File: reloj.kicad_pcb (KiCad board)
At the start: 2 copper layers, 81 parts, among them J1 Conn_01x03, J2 USB_B_Mini, SW1 SW_Push, SW2 SW_Push, SW3 SW_Push, U1 LM555, U10 74LS90, U11 74LS90, U12 74LS90, U13 74LS90, U14 74LS08, U15 74LS47, U16 SA04-11SRWA, U17 74LS47, U18 SA04-11SRWA, U19 74LS47, U2 CD4060B, U20 SA04-11SRWA, U21 74LS47, U22 SA04-11SRWA, U3 74LS90, U4 74LS90, U5 74LS90, U6 74LS90, U7 74LS90, U8 74LS92, U9 74LS92, Y1 32768Hz

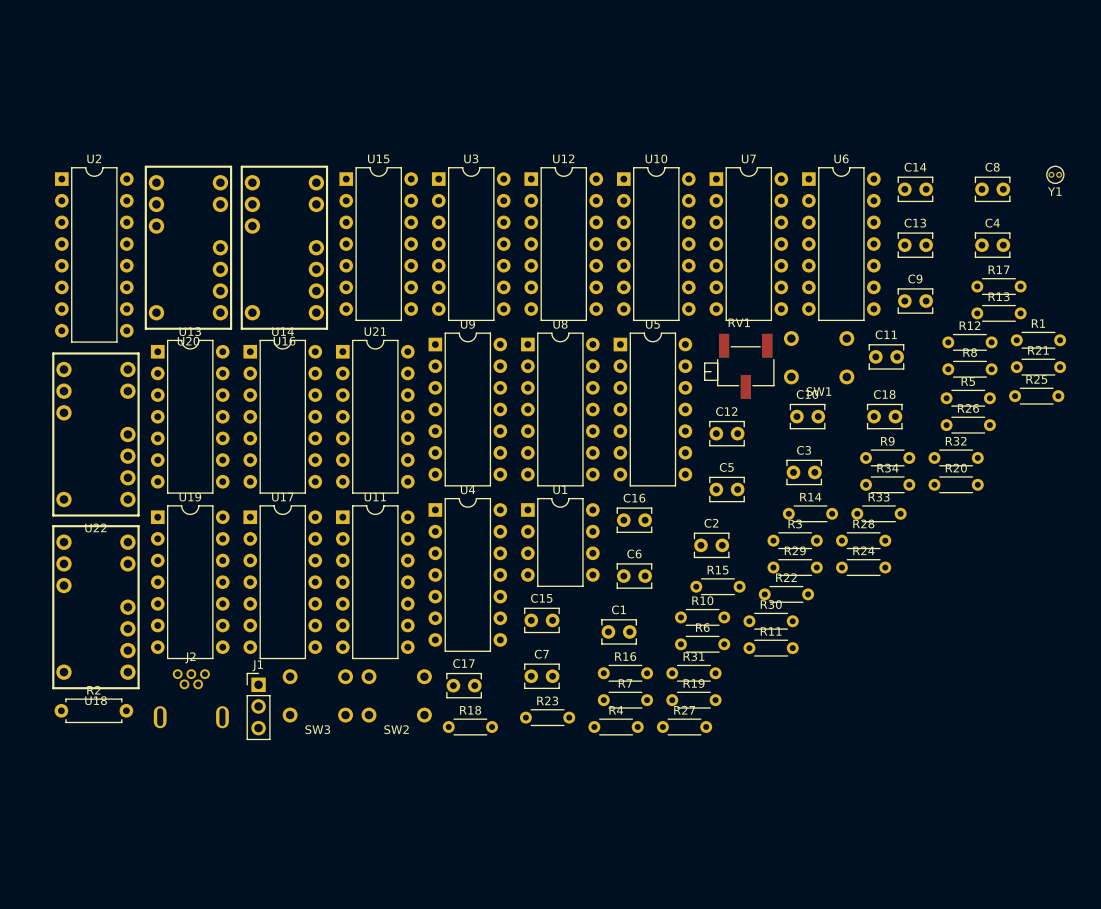
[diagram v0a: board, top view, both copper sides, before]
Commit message: Added most BOM items.
Finished placement on pcb
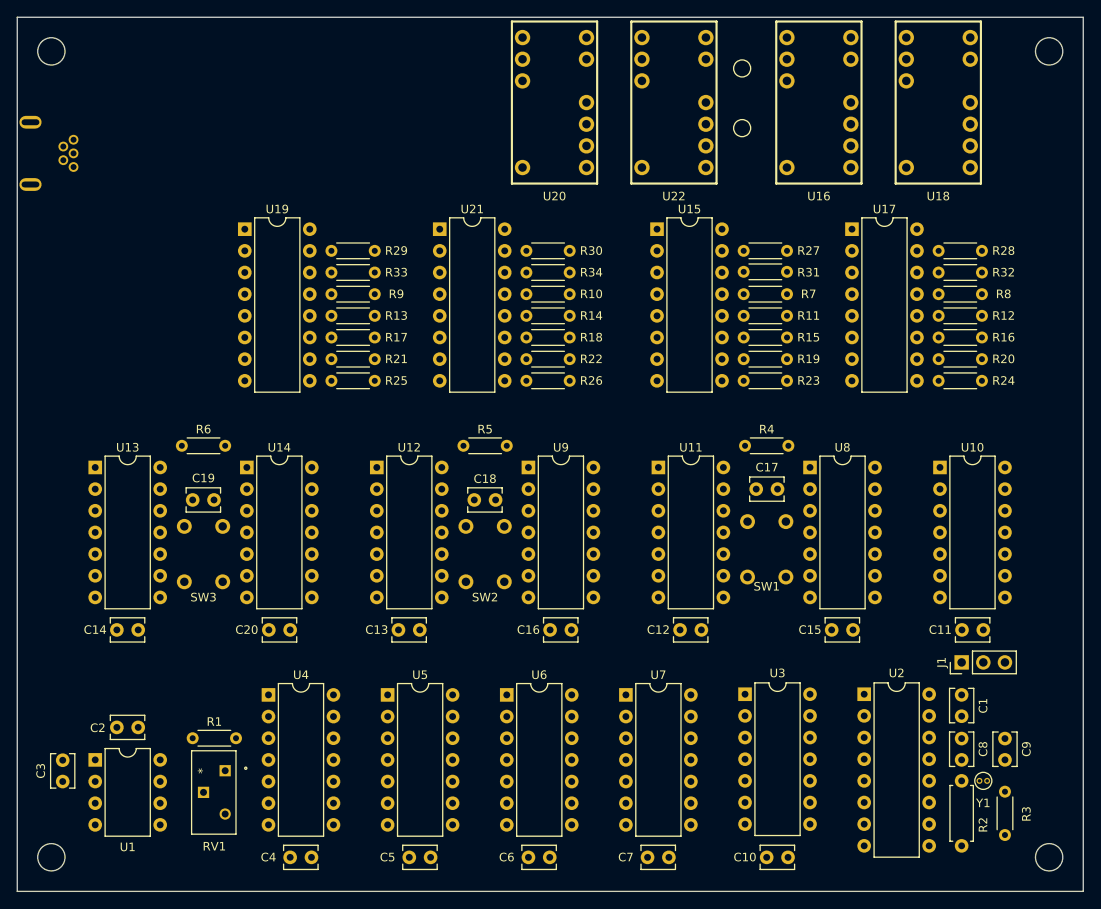
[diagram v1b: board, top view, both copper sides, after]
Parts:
- removed the C12 at (177.0, 93.8)
- removed the C17 at (146.1, 123.4)
- removed the C18 at (195.5, 91.8)
- removed the C8 at (208.1, 65.2)
- added C1: 0.1u, Capacitor_THT:C_Disc_D3.8mm_W2.6mm_P2.50mm, F.Cu at (205.7, 124.5)
- added C10: 0.1u, Capacitor_THT:C_Disc_D3.8mm_W2.6mm_P2.50mm, F.Cu at (182.9, 143.5)
- added C14: 0.1u, Capacitor_THT:C_Disc_D3.8mm_W2.6mm_P2.50mm, F.Cu at (106.7, 116.8)
- added C19: 0.1u, Capacitor_THT:C_Disc_D3.8mm_W2.6mm_P2.50mm, F.Cu at (118.1, 101.6)
- added C20: 0.1u, Capacitor_THT:C_Disc_D3.8mm_W2.6mm_P2.50mm, F.Cu at (124.5, 116.8)
- added C9: 22pf, Capacitor_THT:C_Disc_D3.8mm_W2.6mm_P2.50mm, F.Cu at (210.8, 129.6)
- added REF**: MountingHole_3.2mm_M3, MountingHole:MountingHole_3.2mm_M3, F.Cu at (99.0, 143.5)
- added REF**: MountingHole_3.2mm_M3, MountingHole:MountingHole_3.2mm_M3, F.Cu at (99.0, 49.0)
- added REF**: MountingHole_3.2mm_M3, MountingHole:MountingHole_3.2mm_M3, F.Cu at (216.0, 49.0)
- added REF**: MountingHole_3.2mm_M3, MountingHole:MountingHole_3.2mm_M3, F.Cu at (216.0, 143.5)
- J2: moved to B.Cu
- RV1: footprint Potentiometer_SMD:Potentiometer_Bourns_3269X_Horizontal -> ultra_librarian:3296Y-1-102LF
- U15, U17, U19, U21: footprint Package_DIP:DIP-14_W7.62mm -> Package_DIP:DIP-16_W7.62mm
- moved U18 115.1 mm to (203.0, 55.0)
- moved U2 111.8 mm to (194.3, 124.4)
- moved R1 107.3 mm to (115.6, 129.5)
- moved R2 105.9 mm to (205.7, 134.5), turned to 270 degrees
- moved C5 98.3 mm to (141.0, 143.5)
- moved J1 82.5 mm to (205.7, 120.7), turned to 90 degrees
- moved C3 79.8 mm to (100.3, 134.6), turned to 90 degrees
- moved RV1 79.4 mm to (116.7, 133.4), turned to 90 degrees
- moved U17 78.2 mm to (192.9, 69.8)
- moved U22 78.2 mm to (172.0, 55.0)
- moved R21 75.3 mm to (136.9, 85.1), turned to 180 degrees
- moved R25 75.1 mm to (136.9, 87.6), turned to 180 degrees
- moved C4 74.3 mm to (127.0, 143.5)
- moved Y1 71.6 mm to (208.3, 134.5), turned to 180 degrees
- moved R17 70.9 mm to (136.9, 82.5), turned to 180 degrees
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- renumbered C9 to C11, C10 to C12, C11 to C13, C13 to C15, C14 to C16, C15 to C17, C16 to C18, C1 to C2, C2 to C3, C3 to C4, C4 to C5, C5 to C6, C6 to C7, C7 to C8
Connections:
- R27 pad 2: (no net) -> Net-(R27-Pad2)
- R28 pad 2: (no net) -> Net-(R28-Pad2)
- R29 pad 2: (no net) -> Net-(R29-Pad2)
- R30 pad 2: (no net) -> Net-(R30-Pad2)
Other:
- board outline added: 125 x 102.5 mm
- net class Default: clearance 0.2 -> 0.1524; trace_width 0.25 -> 0.1524; via_dia 0.8 -> 0.508; via_drill 0.4 -> 0.254
- rule trace_clearance: 0.2 -> 0.1524
- rule trace_min: 0.2 -> 0.1524
- rule via_min_drill: 0.3 -> 0.254
- rule via_min_size: 0.4 -> 0.508

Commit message: layout updates
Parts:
- removed the REF** at (99.0, 143.5)
- removed the REF** at (99.0, 49.0)
- removed the REF** at (216.0, 49.0)
- removed the REF** at (216.0, 143.5)
- added REF**: MountingHole_3.2mm_M3, MountingHole:MountingHole_3.2mm_M3, F.Cu at (100.0, 142.5)
- added REF**: MountingHole_3.2mm_M3, MountingHole:MountingHole_3.2mm_M3, F.Cu at (100.0, 50.0)
- added REF**: MountingHole_3.2mm_M3, MountingHole:MountingHole_3.2mm_M3, F.Cu at (215.0, 142.5)
- added REF**: MountingHole_3.2mm_M3, MountingHole:MountingHole_3.2mm_M3, F.Cu at (215.0, 50.0)
- moved J2 23.1 mm to (102.0, 84.0)
- moved C7 2.50 mm to (168.9, 143.5), turned to 0 degrees
- moved R3 1.19 mm to (210.8, 139.7)
- moved U16 1.00 mm to (189.0, 56.0)
- moved U18 1.00 mm to (203.0, 56.0)
- moved U20 1.00 mm to (158.0, 56.0)
- moved U22 1.00 mm to (172.0, 56.0)
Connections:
- U15 pad 6: /DM_Q2 -> /DM_Q3
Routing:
- net GND: track 0.00 -> 667.2 mm
- net CA: track 0.00 -> 653.4 mm, vias 0 -> 1
- net /T_RST: track 0.00 -> 153.5 mm, vias 0 -> 7
- net /H_Q2: track 0.00 -> 75.0 mm, vias 0 -> 1
- net /CLK_DHR: track 0.00 -> 62.9 mm, vias 0 -> 4
- net /DH_Q2: track 0.00 -> 57.9 mm
- net /M_Q1: track 0.00 -> 57.0 mm, vias 0 -> 2
- net /CLK_DMIN: track 0.00 -> 53.7 mm
- net /DH_Q1: track 0.00 -> 53.7 mm
- net /M_Q2: track 0.00 -> 53.4 mm
- net /H_Q1: track 0.00 -> 51.2 mm
- net /CLK_10KHZ: track 0.00 -> 49.8 mm
- net /DM_Q3: track 0.00 -> 48.1 mm
- net Net-(R13-Pad1): track 0.00 -> 47.9 mm, vias 0 -> 2
- net Net-(R17-Pad1): track 0.00 -> 45.6 mm
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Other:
- outline, holes or cut-outs redrawn

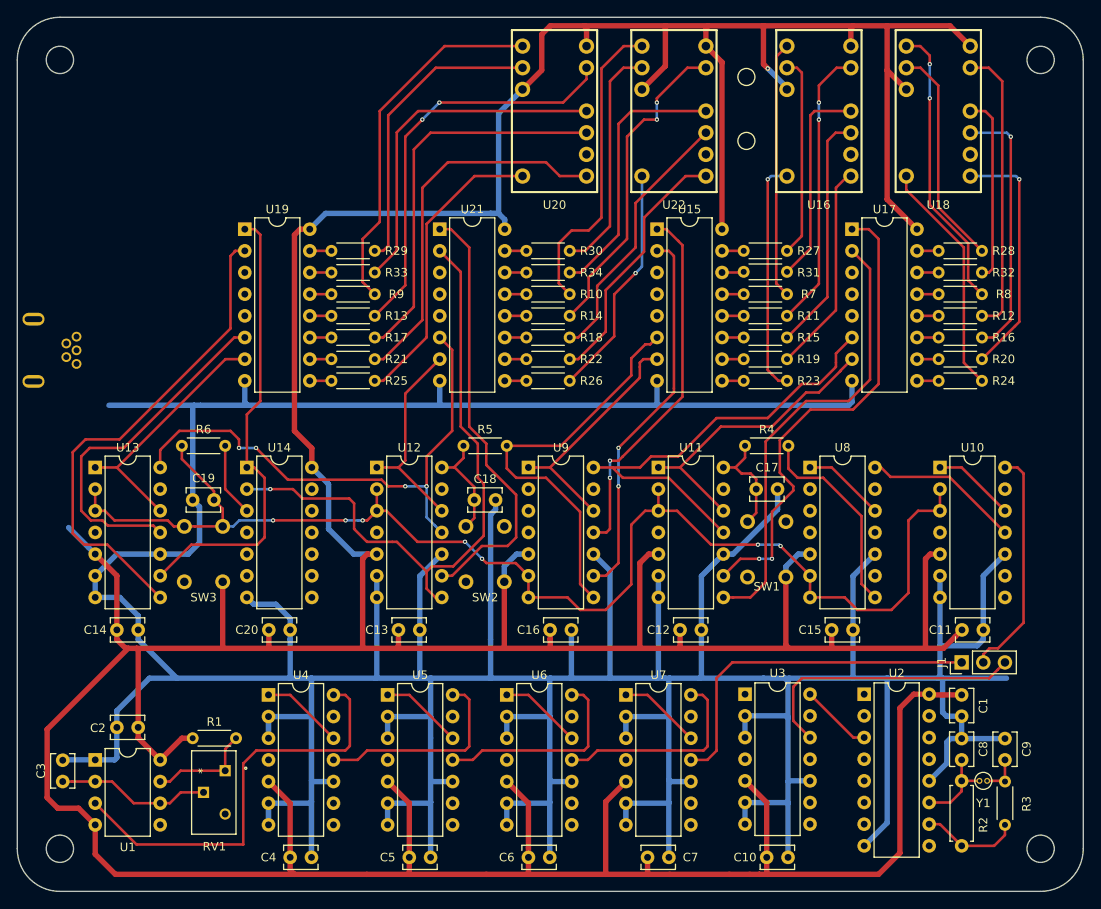
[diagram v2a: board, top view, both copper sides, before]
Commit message: Added 4.7uF cap and cleaned up traces/silkscreen
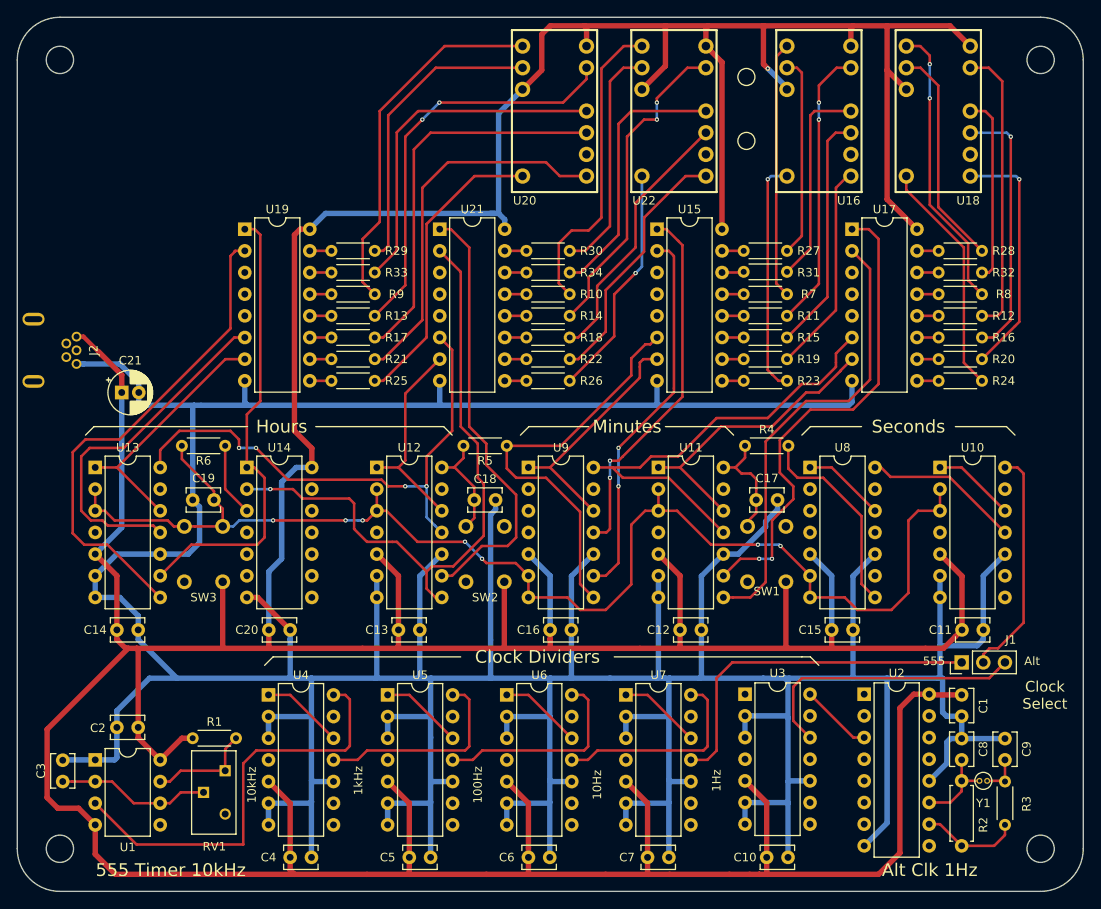
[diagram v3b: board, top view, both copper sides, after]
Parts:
- added C21: 4.7uF, Capacitor_THT:CP_Radial_D5.0mm_P2.00mm, F.Cu at (107.2, 89.0)
- J2: moved to F.Cu
- moved C17 1.27 mm to (181.7, 101.6)
- moved SW1 0.56 mm to (182.9, 108.0)
- turned J2 to 270 degrees
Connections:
- J2 pad 2: (no net) -> Net-(J2-Pad2)
- J2 pad 3: (no net) -> Net-(J2-Pad3)
- J2 pad 4: (no net) -> Net-(J2-Pad4)
- RV1 pad 3: (no net) -> Net-(RV1-Pad3)
- U1 pad 5: (no net) -> Net-(U1-Pad5)
- U10 pad 8: (no net) -> Net-(U10-Pad8)
- U10 pad 9: (no net) -> Net-(U10-Pad9)
- U15 pad 3: (no net) -> Net-(U15-Pad3)
- U15 pad 4: (no net) -> Net-(U15-Pad4)
- U15 pad 5: (no net) -> Net-(U15-Pad5)
- U16 pad 9: (no net) -> Net-(U16-Pad9)
- U17 pad 3: (no net) -> Net-(U17-Pad3)
- U17 pad 4: (no net) -> Net-(U17-Pad4)
- U17 pad 5: (no net) -> Net-(U17-Pad5)
- U18 pad 9: (no net) -> Net-(U18-Pad9)
- U19 pad 3: (no net) -> Net-(U19-Pad3)
- U19 pad 4: (no net) -> Net-(U19-Pad4)
- U19 pad 5: (no net) -> Net-(U19-Pad5)
- U2 pad 1: (no net) -> Net-(U2-Pad1)
- U2 pad 13: (no net) -> Net-(U2-Pad13)
- U2 pad 14: (no net) -> Net-(U2-Pad14)
- U2 pad 15: (no net) -> Net-(U2-Pad15)
- U2 pad 2: (no net) -> Net-(U2-Pad2)
- U2 pad 4: (no net) -> Net-(U2-Pad4)
- U2 pad 5: (no net) -> Net-(U2-Pad5)
- U2 pad 6: (no net) -> Net-(U2-Pad6)
- U2 pad 7: (no net) -> Net-(U2-Pad7)
- U2 pad 9: (no net) -> Net-(U2-Pad9)
- U20 pad 9: (no net) -> Net-(U20-Pad9)
- U21 pad 3: (no net) -> Net-(U21-Pad3)
- U21 pad 4: (no net) -> Net-(U21-Pad4)
- U21 pad 5: (no net) -> Net-(U21-Pad5)
- U22 pad 9: (no net) -> Net-(U22-Pad9)
- U3 pad 1: (no net) -> Net-(U3-Pad1)
- U3 pad 11: (no net) -> Net-(U3-Pad11)
- U3 pad 8: (no net) -> Net-(U3-Pad8)
- U3 pad 9: (no net) -> Net-(U3-Pad9)
- U4 pad 8: (no net) -> Net-(U4-Pad8)
- U4 pad 9: (no net) -> Net-(U4-Pad9)
- U5 pad 8: (no net) -> Net-(U5-Pad8)
- U5 pad 9: (no net) -> Net-(U5-Pad9)
- U6 pad 8: (no net) -> Net-(U6-Pad8)
- U6 pad 9: (no net) -> Net-(U6-Pad9)
- U7 pad 8: (no net) -> Net-(U7-Pad8)
- U7 pad 9: (no net) -> Net-(U7-Pad9)
- U8 pad 11: (no net) -> Net-(U8-Pad11)
- U8 pad 9: (no net) -> Net-(U8-Pad9)
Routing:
- net CA: track 653.4 -> 685.6 mm
- net GND: track 667.2 -> 659.8 mm
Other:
- board text added: "100Hz"
- board text added: "10Hz"
- board text added: "10kHz"
- board text added: "1Hz"
- board text added: "1kHz"
- board text added: "555"
- board text added: "555 Timer 10kHz"
- board text added: "Alt"
- board text added: "Alt Clk 1Hz"
- board text added: "Clock Dividers"
- board text added: "Clock Select"
- board text added: "Hours"
- board text added: "Minutes"
- board text added: "Seconds"

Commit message: Finished layout and labels
DRC passed and verified that remaining non-connected items are
connected externally by components
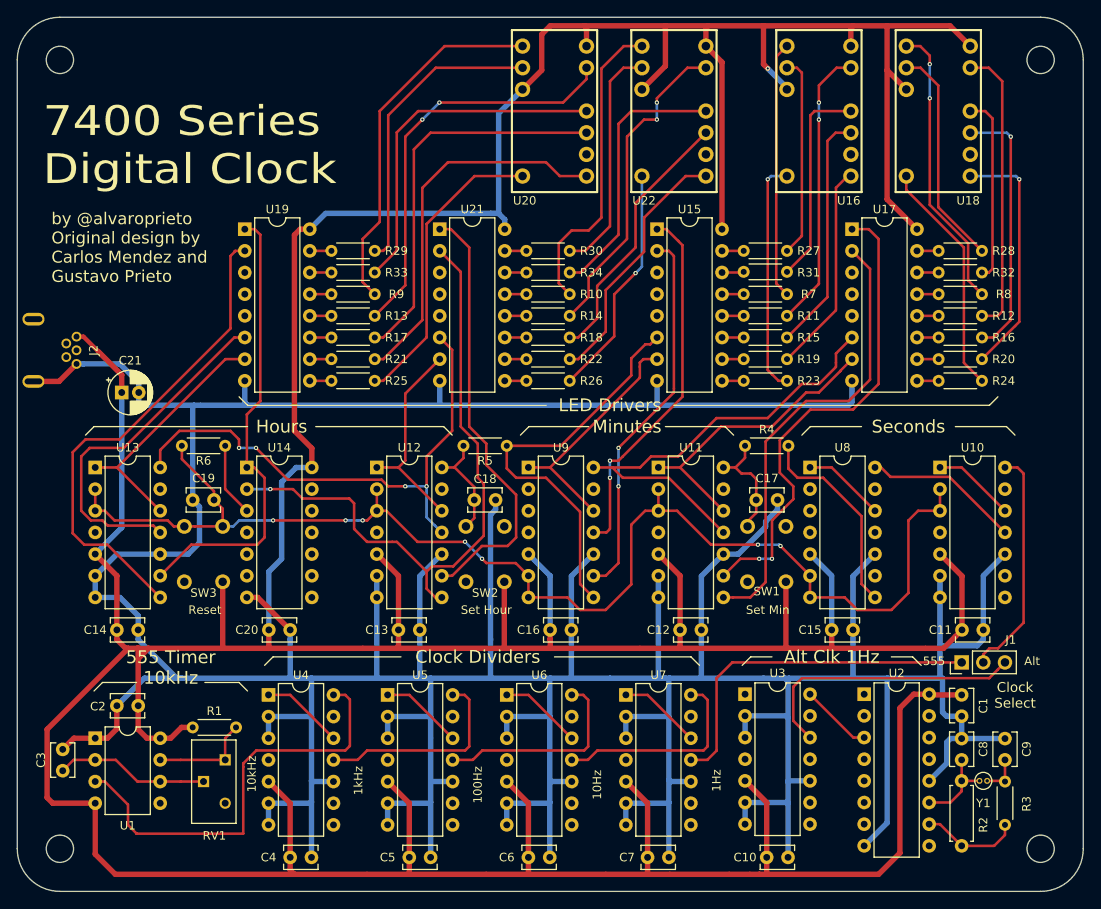
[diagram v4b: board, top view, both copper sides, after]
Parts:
- moved U1 2.54 mm to (104.1, 129.5)
- moved C2 2.54 mm to (109.2, 125.7)
- moved C3 1.27 mm to (100.3, 133.3)
- moved RV1 1.27 mm to (116.7, 132.1)
- moved R1 1.27 mm to (115.6, 128.3)
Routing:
- net GND: track 659.8 -> 664.1 mm
- net CA: track 685.6 -> 686.6 mm
- net /CLK_10KHZ: track 49.8 -> 50.5 mm
- net Net-(R1-Pad2): track 12.5 -> 12.0 mm
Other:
- board text added: "7400 Series Digital Clock"
- board text added: "LED Drivers"
- board text added: "Reset"
- board text added: "Set Hour"
- board text added: "Set Min"
- board text added: "by @alvaroprieto Original design by Carlos Mendez and Gustavo Prieto"

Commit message: Added OSWH logo and changed title to be on copper layer
Released to oshpark
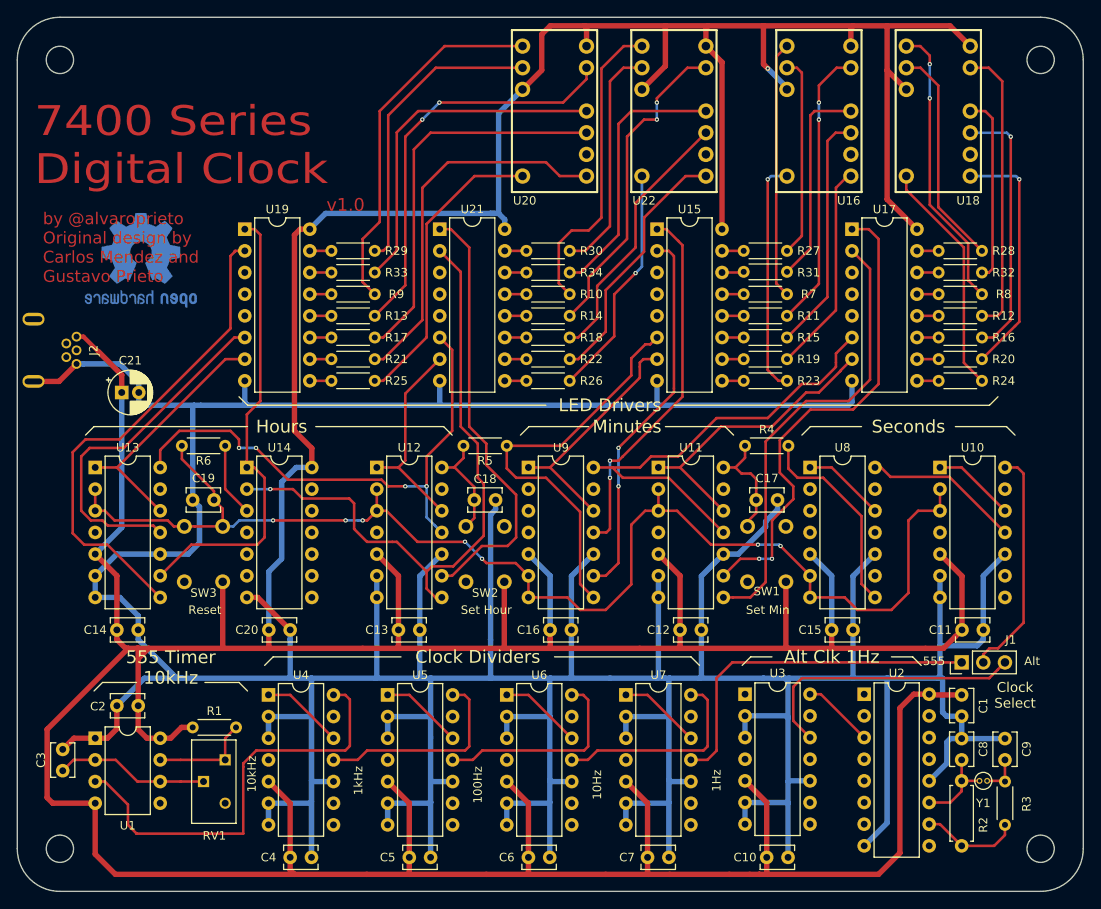
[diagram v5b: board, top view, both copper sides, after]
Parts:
- added REF**: OSHW-Logo2_14.6x12mm_Copper, Symbol:OSHW-Logo2_14.6x12mm_Copper, B.Cu at (109.5, 73.5)
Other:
- board text added: "v1.0"
